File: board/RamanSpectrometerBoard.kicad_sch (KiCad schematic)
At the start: 0 parts

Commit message: Potential Schematic Layout + Basic Power Circuits
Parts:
- added H1, H2, H3, H4: MountingHole, symbol Mechanical:MountingHole
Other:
- added sheet 12v-5v OKI (oki.kicad_sch)
- added sheet CCD Breakout (CCDBreakout.kicad_sch)
- added sheet CCD Clocks (CCDClocks.kicad_sch)
- added sheet Diode Connector (diodeConnector.kicad_sch)
- added sheet Ethernet (ethernet.kicad_sch)
- added sheet Fan Connector (fanConnector.kicad_sch)
- added sheet Gantry Connector (gantryConnector.kicad_sch)
- added sheet Limi Switches (limitSwitches.kicad_sch)
- added sheet Motor Encoder (motorEncoder.kicad_sch)
- added sheet Power Led's (powerLeds.kicad_sch)
- added sheet Servo Ports (servos.kicad_sch)
- added sheet TOF Sensor (TOFSensor.kicad_sch)
- added sheet Teensy (teensy.kicad_sch)

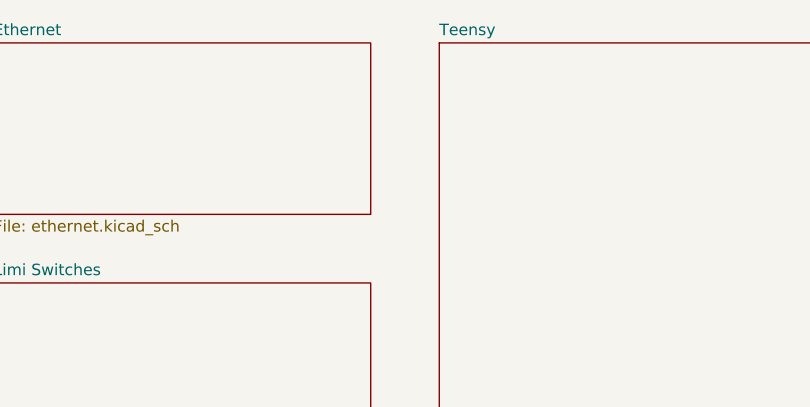
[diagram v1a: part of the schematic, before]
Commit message: Added Ethernet
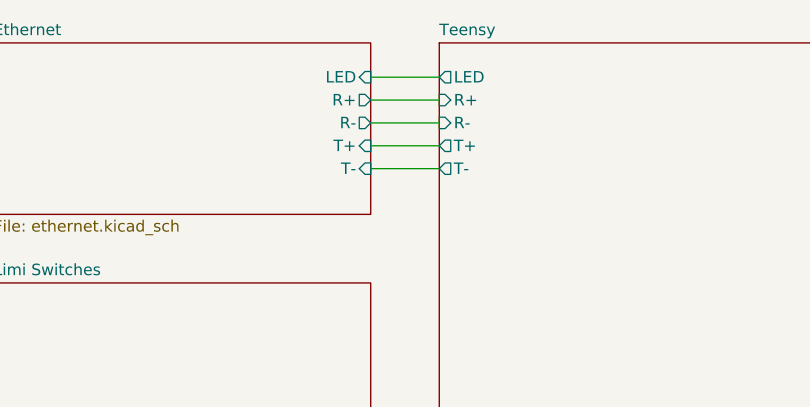
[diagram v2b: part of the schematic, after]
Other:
- sheet Ethernet ports: added LED, R+, R-, T+, T-; removed none
- sheet Teensy ports: added LED, R+, R-, T+, T-; removed none
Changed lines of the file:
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@@
 	(generator_version "9.0")
 	(paper "A4")
+	(wire
+		(pts
+			(xy 60.96 25.4) (xy 68.58 25.4)
+		)
+		(stroke
+			(width 0)
+			(type default)
+		)
+	)
+	(wire
+		(pts
+			(xy 60.96 33.02) (xy 68.58 33.02)
+		)
+		(stroke
+			(width 0)
+			(type default)
+		)
+	)
+	(wire
+		(pts
+			(xy 60.96 27.94) (xy 68.58 27.94)
+		)
+		(stroke
+			(width 0)
+			(type default)
+		)
+	)
+	(wire
+		(pts
+			(xy 60.96 30.48) (xy 68.58 30.48)
+		)
+		(stroke
+			(width 0)
+			(type default)
+		)
+	)
+	(wire
+		(pts
+			(xy 60.96 22.86) (xy 68.58 22.86)
+		)
+		(stroke
+			(width 0)
+			(type default)
+		)
+	)
 	(symbol
 		(lib_id "Mechanical:MountingHole")
@@
 			)
 		)
+		(pin "LED" input
+			(at 60.96 22.86 0)
+			(effects
+				(font
+					(size 1.27 1.27)
+				)
+				(justify right)
+			)
+		)
+		(pin "R+" output
+			(at 60.96 25.4 0)
+			(effects
+				(font
+					(size 1.27 1.27)
+				)
+				(justify right)
+			)
+		)
+		(pin "R-" output
+			(at 60.96 27.94 0)
+			(effects
+				(font
+					(size 1.27 1.27)
+				)
+				(justify right)
+			)
+		)
+		(pin "T+" input
+			(at 60.96 30.48 0)
+			(effects
+				(font
+					(size 1.27 1.27)
+				)
+				(justify right)
+			)
+		)
+		(pin "T-" input
+			(at 60.96 33.02 0)
+			(effects
+				(font
+					(size 1.27 1.27)
+				)
+				(justify right)
+			)
+		)
 		(instances
 			(project "RamanSpectrometerBoard"
@@
 			)
 		)
+		(pin "LED" output
+			(at 68.58 22.86 180)
+			(effects
+				(font
+					(size 1.27 1.27)
+				)
+				(justify left)
+			)
+		)
+		(pin "R+" input
+			(at 68.58 25.4 180)
+			(effects
+				(font
+					(size 1.27 1.27)
+				)
+				(justify left)
+			)
+		)
+		(pin "R-" input
+			(at 68.58 27.94 180)
+			(effects
+				(font
+					(size 1.27 1.27)
+				)
+				(justify left)
+			)
+		)
+		(pin "T+" output
+			(at 68.58 30.48 180)
+			(effects
+				(font
+					(size 1.27 1.27)
+				)
+				(justify left)
+			)
+		)
+		(pin "T-" output
+			(at 68.58 33.02 180)
+			(effects
+				(font
+					(size 1.27 1.27)
+				)
+				(justify left)
+			)
+		)

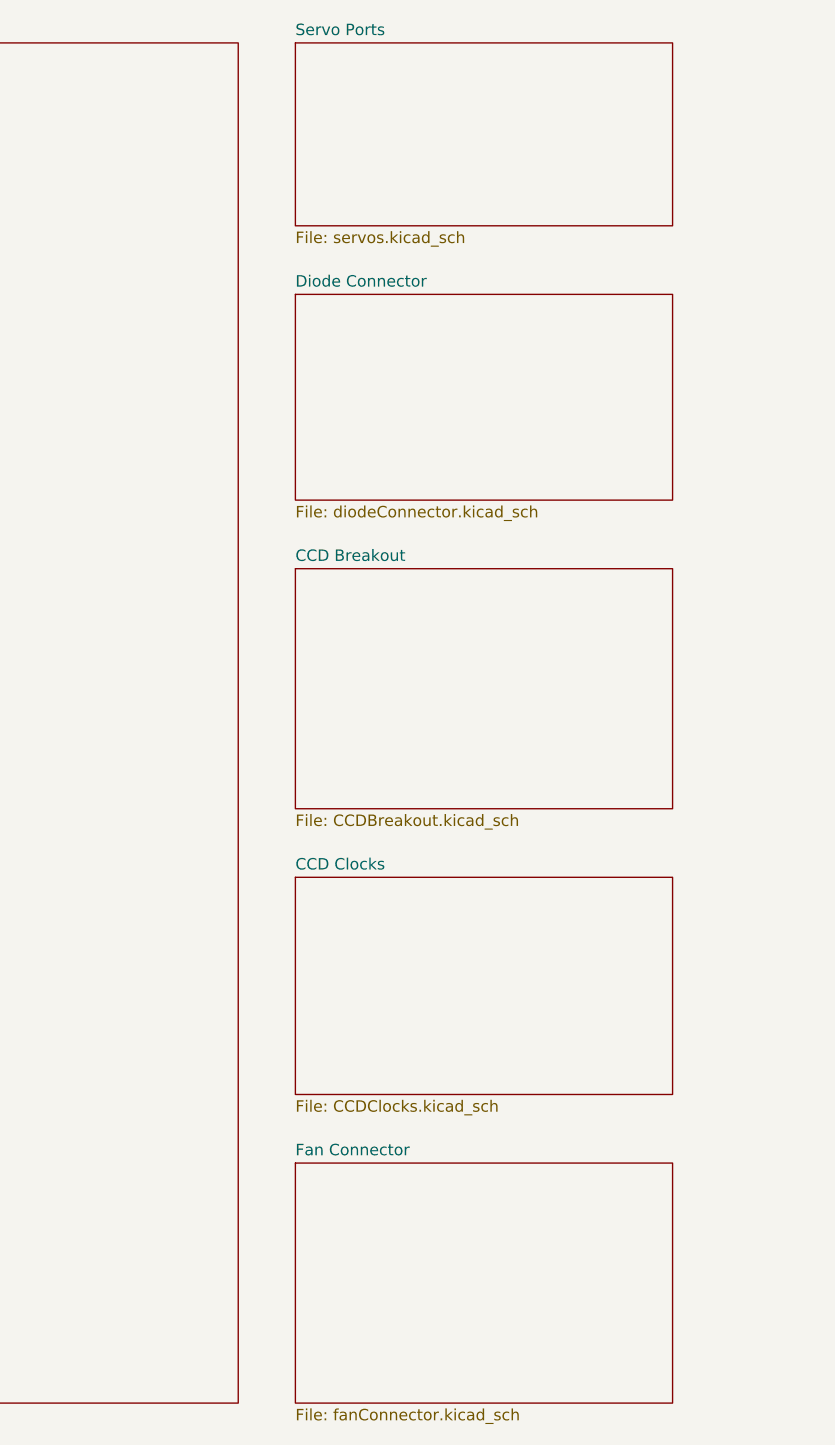
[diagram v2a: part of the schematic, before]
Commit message: Added CAN Transceiver
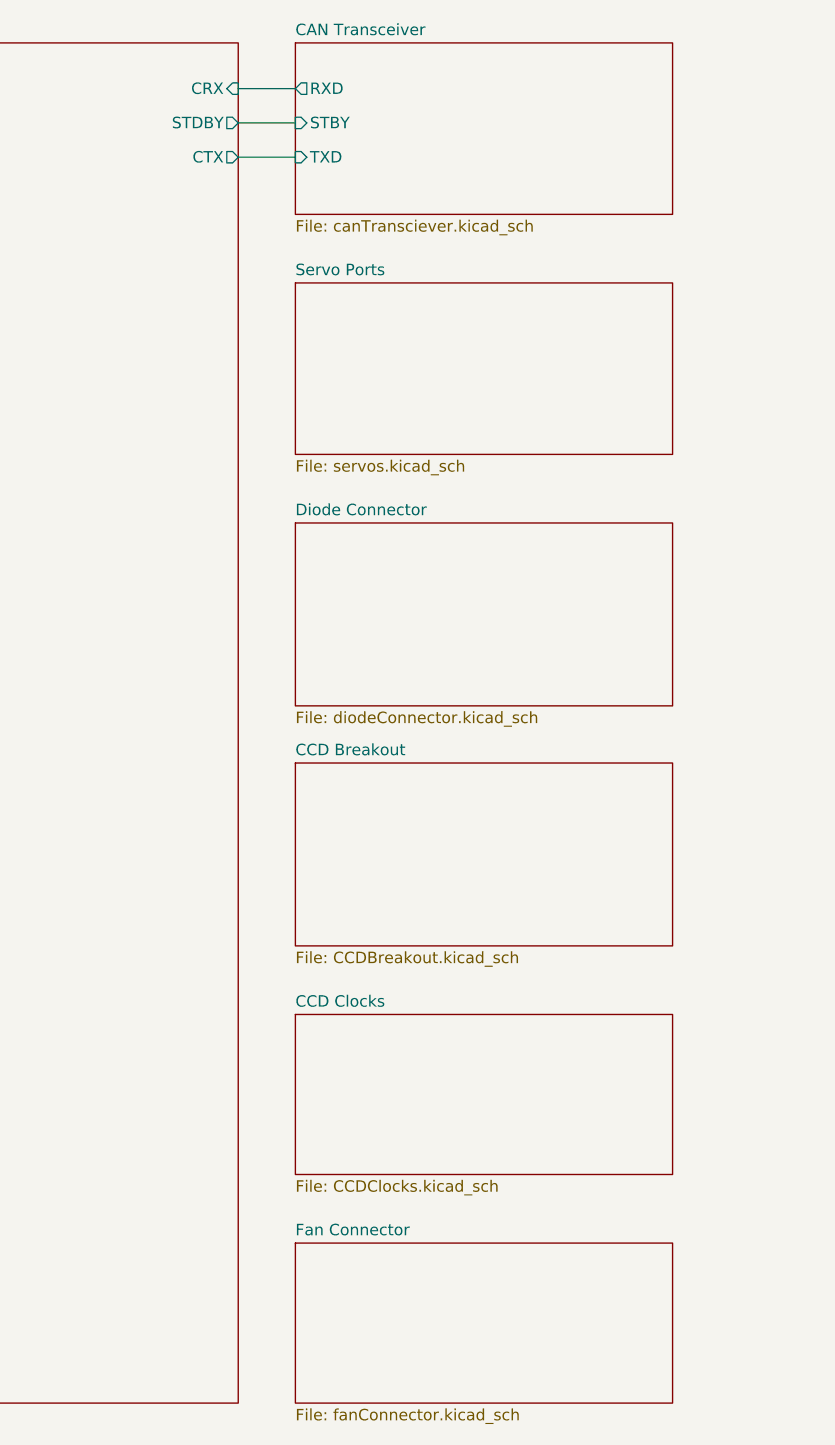
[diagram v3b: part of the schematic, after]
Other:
- added sheet CAN Transceiver (canTransciever.kicad_sch)
- sheet Teensy ports: added CRX, CTX, STDBY; removed none
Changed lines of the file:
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@@
+	(wire
+		(pts
+			(xy 127 27.94) (xy 133.35 27.94)
+		)
+		(stroke
+			(width 0)
+			(type default)
+		)
+	)
 	(wire
 		(pts
@@
 	(wire
 		(pts
+			(xy 127 24.13) (xy 133.35 24.13)
+		)
+		(stroke
+			(width 0)
+			(type default)
+		)
+	)
+	(wire
+		(pts
 			(xy 60.96 22.86) (xy 68.58 22.86)
+		)
+		(stroke
+			(width 0)
+			(type default)
+		)
+	)
+	(wire
+		(pts
+			(xy 127 31.75) (xy 133.35 31.75)
 		)
 		(stroke
@@
 	)
 	(sheet
+		(at 133.35 19.05)
+		(size 41.91 19.05)
+		(exclude_from_sim no)
+		(in_bom yes)
+		(on_board yes)
+		(dnp no)
+		(fields_autoplaced yes)
+		(stroke
+			(width 0.1524)
+			(type solid)
+		)
+		(fill
+			(color 0 0 0 0.0000)
+		)
+		(property "Sheetname" "CAN Transceiver"
+			(at 133.35 18.3384 0)
+			(effects
+				(font
+					(size 1.27 1.27)
+				)
+				(justify left bottom)
+			)
+		)
+		(property "Sheetfile" "canTransciever.kicad_sch"
+			(at 133.35 38.6846 0)
+			(effects
+				(font
+					(size 1.27 1.27)
+				)
+				(justify left top)
+			)
+		)
+		(pin "RXD" output
+			(at 133.35 24.13 180)
+			(effects
+				(font
+					(size 1.27 1.27)
+				)
+				(justify left)
+			)
+		)
+		(pin "STBY" input
+			(at 133.35 27.94 180)
+			(effects
+				(font
+					(size 1.27 1.27)
+				)
+				(justify left)
+			)
+		)
+		(pin "TXD" input
+			(at 133.35 31.75 180)
+			(effects
+				(font
+					(size 1.27 1.27)
+				)
+				(justify left)
+			)
+		)
+		(instances
+			(project "RamanSpectrometerBoard"
+				(path "/ab487c59-f066-48f5-a383-99e8eaf806bf"
+					(page "15")
+				)
+			)
+		)
+	)
+	(sheet
 		(at 19.05 45.72)
 		(size 41.91 22.86)
@@
 	)
 	(sheet
-		(at 133.35 77.47)
-		(size 41.91 26.67)
+		(at 133.35 99.06)
+		(size 41.91 20.32)
 		(exclude_from_sim no)
 		(in_bom yes)
@@
 		)
 		(property "Sheetname" "CCD Breakout"
-			(at 133.35 76.7584 0)
+			(at 133.35 98.3484 0)
 			(effects
 				(font
@@
 		)
 		(property "Sheetfile" "CCDBreakout.kicad_sch"
-			(at 133.35 104.7246 0)
+			(at 133.35 119.9646 0)
 			(effects
 				(font
@@
 	)
 	(sheet
-		(at 133.35 111.76)
-		(size 41.91 24.13)
+		(at 133.35 127)
+		(size 41.91 17.78)
 		(exclude_from_sim no)
 		(in_bom yes)
@@
 		)
 		(property "Sheetname" "CCD Clocks"
-			(at 133.35 111.0484 0)
+			(at 133.35 126.2884 0)
 			(effects
 				(font
@@
 		)
 		(property "Sheetfile" "CCDClocks.kicad_sch"
-			(at 133.35 136.4746 0)
+			(at 133.35 145.3646 0)
 			(effects
 				(font
@@
 	)
 	(sheet
-		(at 133.35 143.51)
-		(size 41.91 26.67)
+		(at 133.35 152.4)
+		(size 41.91 17.78)
 		(exclude_from_sim no)
 		(in_bom yes)
@@
 		)
 		(property "Sheetname" "Fan Connector"
-			(at 133.35 142.7984 0)
+			(at 133.35 151.6884 0)
 			(effects
 				(font
@@
 	)
 	(sheet
-		(at 133.35 46.99)
-		(size 41.91 22.86)
+		(at 133.35 72.39)
+		(size 41.91 20.32)
 		(exclude_from_sim no)
 		(in_bom yes)
@@
 		)
 		(property "Sheetname" "Diode Connector"
-			(at 133.35 46.2784 0)
+			(at 133.35 71.6784 0)
 			(effects
 				(font
@@
 		)
 		(property "Sheetfile" "diodeConnector.kicad_sch"
-			(at 133.35 70.4346 0)
+			(at 133.35 93.2946 0)
 			(effects
 				(font
@@
 	)
 	(sheet
-		(at 133.35 19.05)
-		(size 41.91 20.32)
+		(at 133.35 45.72)
+		(size 41.91 19.05)
 		(exclude_from_sim no)
 		(in_bom yes)
@@
 		)
 		(property "Sheetname" "Servo Ports"
-			(at 133.35 18.3384 0)
+			(at 133.35 45.0084 0)
 			(effects
 				(font
@@
 		)
 		(property "Sheetfile" "servos.kicad_sch"
-			(at 133.35 39.9546 0)
+			(at 133.35 65.3546 0)
 			(effects
 				(font
@@
 			)
 		)
+		(pin "CRX" input
+			(at 127 24.13 0)
+			(effects
+				(font
+					(size 1.27 1.27)
+				)
+				(justify right)
+			)
+		)
+		(pin "CTX" output
+			(at 127 31.75 0)
+			(effects
+				(font
+					(size 1.27 1.27)
+				)
+				(justify right)
+			)
+		)
+		(pin "STDBY" output
+			(at 127 27.94 0)
+			(effects
+				(font
+					(size 1.27 1.27)
+				)
+				(justify right)
+			)
+		)
